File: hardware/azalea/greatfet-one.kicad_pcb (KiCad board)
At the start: 4 copper layers, 70.6 x 53.3 mm, 88 parts, among them J1 NEIGHBOR1, J2 NEIGHBOR2, J3 USB-MICRO-B-SHIELDED, J4 USB-MICRO-B-SHIELDED, J5 JTAG, J7 BONUS_ROW, SW1 DFU, SW2 RESET, U1 LPC4330FBD144, U2 W25Q16DV, U3 AP7333, U4 IP4220CZ6, U5 NX5P2553GV, X1 XTAL4PIN, X2 RTC_XTAL

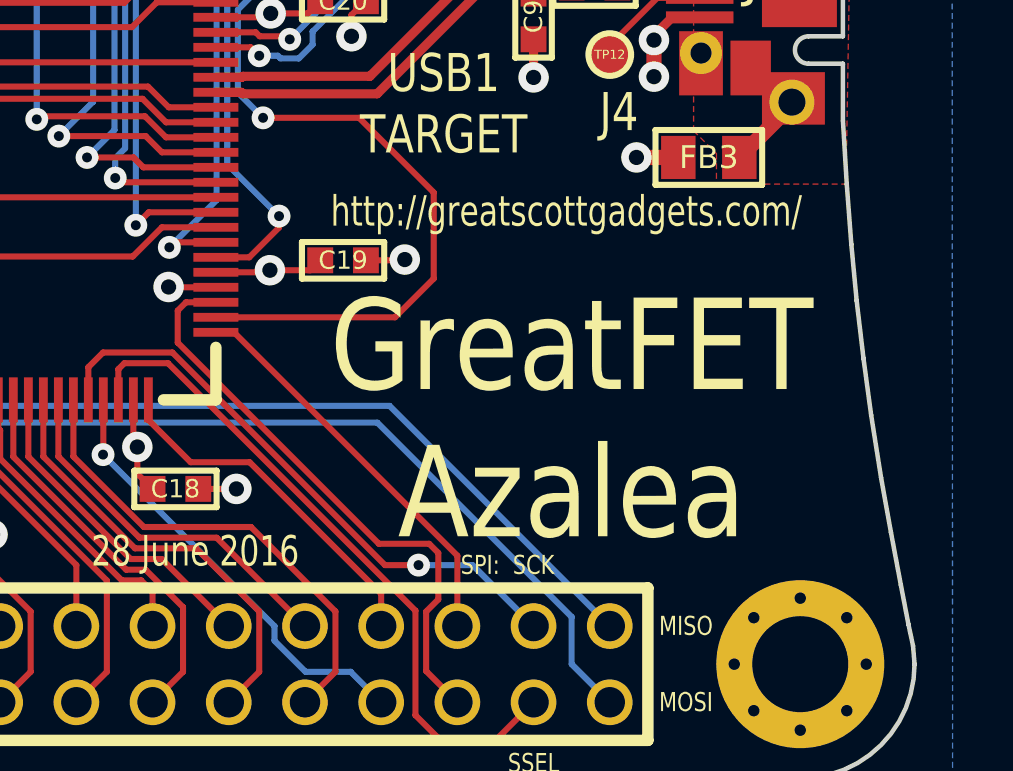
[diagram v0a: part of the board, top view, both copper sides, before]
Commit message: renamed Azalea to GreatFET One
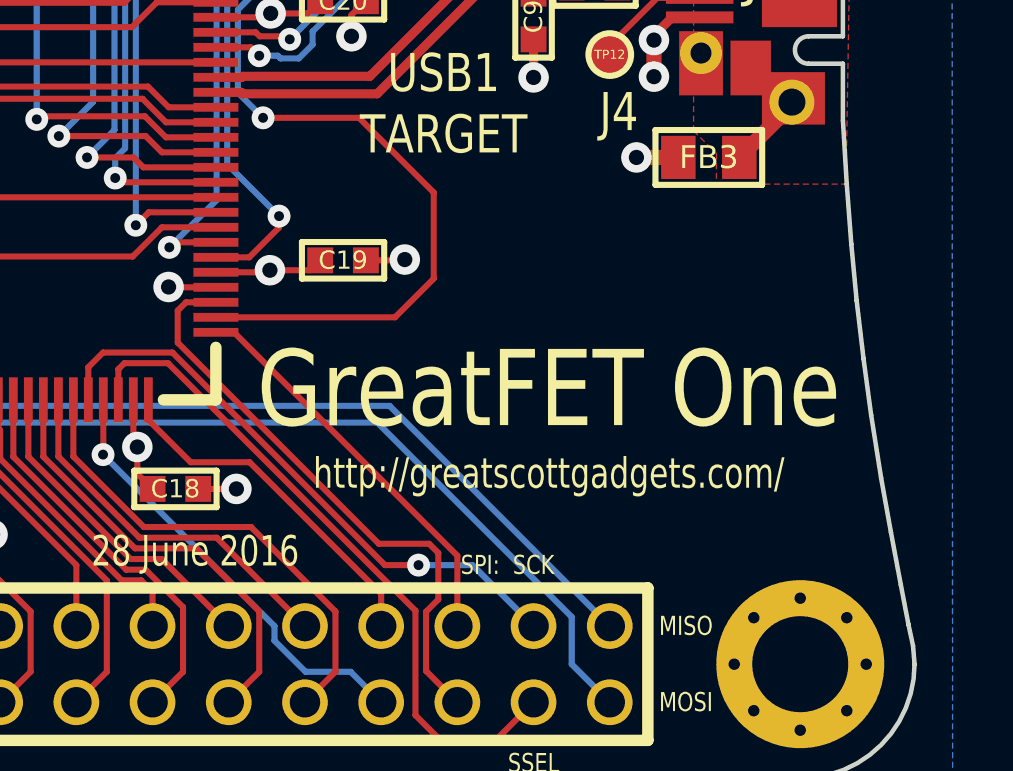
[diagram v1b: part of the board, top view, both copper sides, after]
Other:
- board text added: "GreatFET One"
- board text removed: "GreatFET Azalea"
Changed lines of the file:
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@@
     (links 352)
     (no_connects 0)
-    (area 93.271704 68.58 275.715801 199.465001)
+    (area 93.271704 68.58 207.466001 199.465001)
     (thickness 1.6)
     (drawings 154)
@@
     (effects (font (size 1.016 0.762) (thickness 0.1524)))
   )
-  (gr_text http://greatscottgadgets.com/ (at 164.9222 105.5624) (layer F.SilkS)
+  (gr_text http://greatscottgadgets.com/ (at 164.338 114.3) (layer F.SilkS)
     (effects (font (size 1.016 0.762) (thickness 0.1524)))
   )
@@
   (gr_arc (start 112.3188 74.93) (end 112.3188 71.12) (angle -70) (layer Cmts.User) (width 0.15))
   (gr_arc (start 172.72 120.65) (end 176.53 120.65) (angle 90) (layer Edge.Cuts) (width 0.15))
-  (gr_text "GreatFET\nAzalea" (at 165.1 112.522) (layer F.SilkS)
-    (effects (font (size 3.048 2.54) (thickness 0.4572)))
+  (gr_text "GreatFET One" (at 164.338 111.506) (layer F.SilkS)
+    (effects (font (size 2.54 2.032) (thickness 0.381)))
   )
   (gr_line (start 108.458 120.904) (end 108.7374 121.9454) (angle 90) (layer Cmts.User) (width 0.15))
